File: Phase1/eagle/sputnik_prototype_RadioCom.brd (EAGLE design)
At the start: 100 x 80 mm, 66 parts, among them Y1 32MHz

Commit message: hooked up SPI cache
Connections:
- new net N$12: U$1.29, U$3.2
- new net N$14: U$1.28, U$3.6
- new net N$15: U$1.31, U$3.5
- new net N$23: U$1.58, U$3.7
- new net N$26: U$1.32, U$3.3
- new net N$4: U$1.27, U$3.1
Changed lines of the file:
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@@
 <?xml version="1.0" encoding="utf-8"?>
 <!DOCTYPE eagle SYSTEM "eagle.dtd">
-<eagle version="7.4.0">
+<eagle version="7.3.0">
 <drawing>
 <settings>
@@
 <wire x1="-72.43" y1="-184.15" x2="-76.67" y2="-201.93" width="0" layer="19" extent="1-1"/>
 </signal>
+<signal name="N$4">
+<contactref element="U$1" pad="27"/>
+<contactref element="U$3" pad="1"/>
+<wire x1="-20.2522" y1="10.37" x2="-68.03" y2="-160.81" width="0" layer="19" extent="1-1"/>
+</signal>
+<signal name="N$12">
+<contactref element="U$3" pad="2"/>
+<contactref element="U$1" pad="29"/>
+<wire x1="-20.88" y1="11.4978" x2="-66.76" y2="-160.81" width="0" layer="19" extent="1-1"/>
+</signal>
+<signal name="N$14">
+<contactref element="U$1" pad="28"/>
+<contactref element="U$3" pad="6"/>
+<wire x1="-20.2522" y1="10.87" x2="-65.49" y2="-155.51" width="0" layer="19" extent="1-1"/>
+</signal>
+<signal name="N$15">
+<contactref element="U$1" pad="31"/>
+<contactref element="U$3" pad="5"/>
+<wire x1="-21.88" y1="11.4978" x2="-64.22" y2="-155.51" width="0" layer="19" extent="1-1"/>
+</signal>
+<signal name="N$23">
+<contactref element="U$1" pad="58"/>
+<contactref element="U$3" pad="7"/>
+<wire x1="-22.38" y1="10.37" x2="-66.76" y2="-155.51" width="0" layer="19" extent="1-1"/>
+</signal>
+<signal name="N$26">
+<contactref element="U$1" pad="32"/>
+<contactref element="U$3" pad="3"/>
+<wire x1="-22.38" y1="11.4978" x2="-65.49" y2="-160.81" width="0" layer="19" extent="1-1"/>
+</signal>
 </signals>

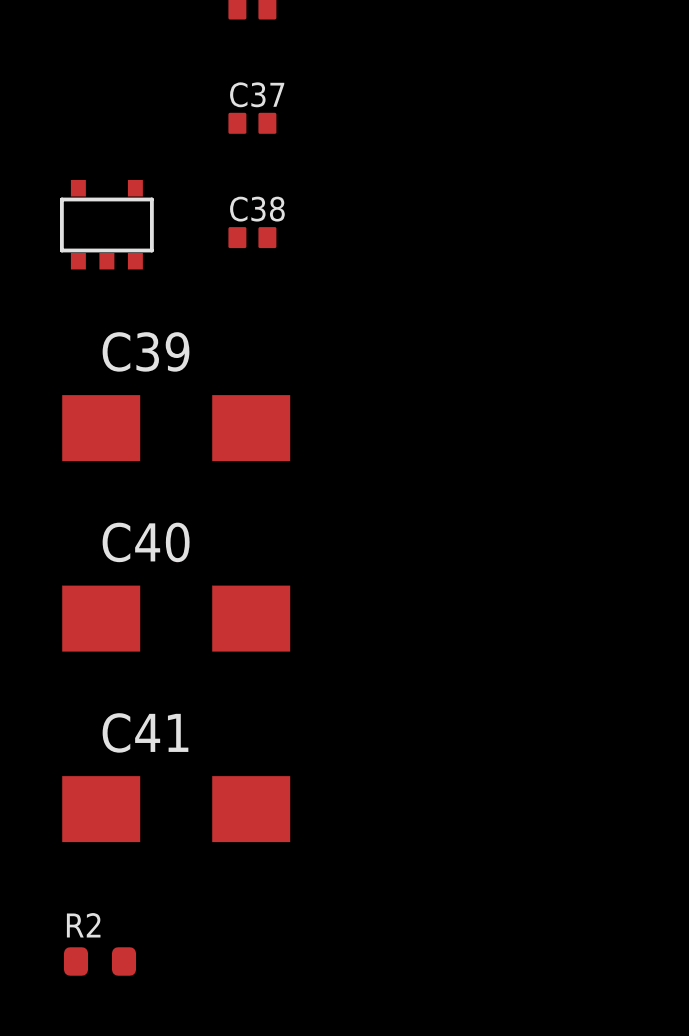
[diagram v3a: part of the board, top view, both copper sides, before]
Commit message: Changed KW0x LDO
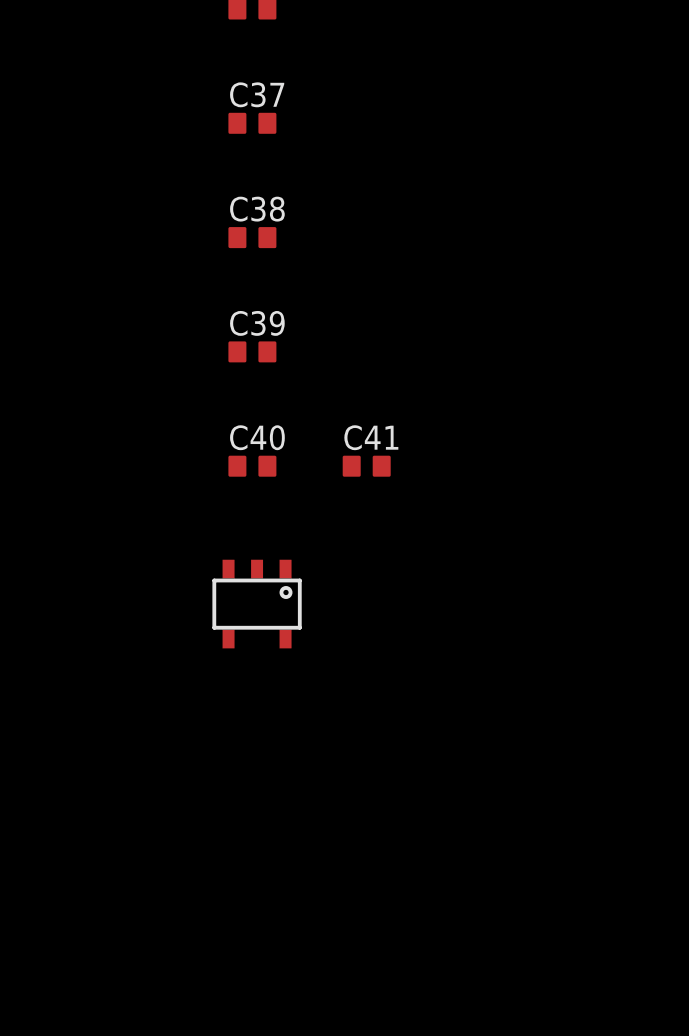
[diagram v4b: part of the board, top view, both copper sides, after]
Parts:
- removed R2: (no value), rcl_custom:.0603-B-NOSILK
- C39: value 4.7uF -> 2.2uF; device rcl:CT6032 -> rcl_custom:.0402-B-NOSILK
- C40: value 1uF -> 10nF; device rcl:CT6032 -> rcl_custom:.0402-B-NOSILK
- C41: value .01uF -> 1uF; device rcl:CT6032 -> rcl_custom:.0402-B-NOSILK
- U$8: value TPS78930DBVT -> AAT3215; device psas_c3_team05:TPS78930DBVT -> psas_c3_team05:AAT3215
- moved U$8 13.7 mm to (-73.7, -189.2)
- moved C41 13.1 mm to (-68.6, -185.4)
- moved C40 5.68 mm to (-72.4, -185.4)
- moved C39 3.59 mm to (-72.4, -181.6)
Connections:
- removed net N$3: C26.1, C27.1, C28.2, C29.2, C39.+, U$1.1, U$1.19, U$1.55, U$1.56, U$8.5
- net 3.3V: no longer C40.+, U$8.1
- net GND: now also C39.2, C40.2, C41.2; no longer C40.-, C41.-, R2.1, U$8.3
- net N$11: now also C26.1, C27.1, C28.2, C29.2, C39.1, U$1.1, U$1.19, U$1.55, U$1.56, U$8.5; no longer C41.+, U$8.4
- net N$13: now also C40.1, U$8.4; no longer C39.-, R2.2
- net V+: now also C41.1, U$8.1
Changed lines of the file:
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@@
 <?xml version="1.0" encoding="utf-8"?>
 <!DOCTYPE eagle SYSTEM "eagle.dtd">
-<eagle version="7.3.0">
+<eagle version="7.4.0">
 <drawing>
 <settings>
@@
 <element name="C37" library="rcl_custom" package=".0402-B-NOSILK" value="10nF" x="-72.39" y="-173.99"/>
 <element name="C38" library="rcl_custom" package=".0402-B-NOSILK" value="1uF" x="-72.39" y="-177.8"/>
-<element name="U$8" library="psas_c3_team05" package="TPS78930DBVT" value="TPS78930DBVT" x="-78.74" y="-176.53"/>
-<element name="C39" library="rcl" package="CT6032" value="4.7uF" x="-74.93" y="-184.15"/>
-<element name="C40" library="rcl" package="CT6032" value="1uF" x="-74.93" y="-190.5"/>
-<element name="C41" library="rcl" package="CT6032" value=".01uF" x="-74.93" y="-196.85"/>
-<element name="R2" library="rcl_custom" package=".0603-B-NOSILK" value="" x="-77.47" y="-201.93"/>
+<element name="U$8" library="psas_c3_team05" package="AAT3215" value="AAT3215" x="-73.66" y="-189.23"/>
+<element name="C39" library="rcl_custom" package=".0402-B-NOSILK" value="2.2uF" x="-72.39" y="-181.61"/>
+<element name="C40" library="rcl_custom" package=".0402-B-NOSILK" value="10nF" x="-72.39" y="-185.42"/>
+<element name="C41" library="rcl_custom" package=".0402-B-NOSILK" value="1uF" x="-68.58" y="-185.42"/>
 </elements>
 <signals>
@@
 <contactref element="U$3" pad="4"/>
 <contactref element="U$8" pad="2"/>
-<contactref element="U$8" pad="3"/>
-<contactref element="C41" pad="-"/>
-<contactref element="C40" pad="-"/>
-<contactref element="R2" pad="1"/>
+<contactref element="C41" pad="2"/>
+<contactref element="C39" pad="2"/>
+<contactref element="C40" pad="2"/>
+<wire x1="-71.89" y1="-185.42" x2="-68.08" y2="-185.42" width="0" layer="19" extent="1-1"/>
+<wire x1="-72.235" y1="-188.85" x2="-71.89" y2="-185.42" width="0" layer="19" extent="1-1"/>
+<wire x1="-71.89" y1="-181.61" x2="-71.89" y2="-185.42" width="0" layer="19" extent="1-1"/>
+<wire x1="-71.89" y1="-177.8" x2="-71.89" y2="-181.61" width="0" layer="19" extent="1-1"/>
 <wire x1="-71.89" y1="-173.99" x2="-71.89" y2="-177.8" width="0" layer="19" extent="1-1"/>
 <wire x1="-71.89" y1="-170.18" x2="-71.89" y2="-173.99" width="0" layer="19" extent="1-1"/>
-<wire x1="-76.29" y1="-178.587" x2="-71.89" y2="-177.8" width="0" layer="19" extent="1-1"/>
-<wire x1="-77.24" y1="-178.587" x2="-76.29" y2="-178.587" width="0" layer="19" extent="1-1"/>
 <wire x1="-72.235" y1="-164.72" x2="-71.89" y2="-170.18" width="0" layer="19" extent="1-1"/>
 <wire x1="-64.77" y1="-166.37" x2="-72.235" y2="-164.72" width="0" layer="19" extent="1-1"/>
@@
 <wire x1="-61.76" y1="-154.94" x2="-61.76" y2="-160.02" width="0" layer="19" extent="1-1"/>
 <wire x1="-60.03" y1="-151.502" x2="-61.76" y2="-154.94" width="0" layer="19" extent="1-1"/>
-<wire x1="-72.43" y1="-190.5" x2="-76.29" y2="-178.587" width="0" layer="19" extent="1-1"/>
-<wire x1="-72.43" y1="-196.85" x2="-72.43" y2="-190.5" width="0" layer="19" extent="1-1"/>
-<wire x1="-78.27" y1="-201.93" x2="-72.43" y2="-196.85" width="0" layer="19" extent="1-1"/>
 <wire x1="-50.84" y1="-129.54" x2="-60.03" y2="-151.502" width="0" layer="19" extent="1-1"/>
 <wire x1="-56.65" y1="-119.38" x2="-50.84" y2="-129.54" width="0" layer="19" extent="1-1"/>
@@
 <contactref element="C38" pad="1"/>
 <contactref element="U$7" pad="1"/>
+<contactref element="C41" pad="1"/>
+<contactref element="U$8" pad="1"/>
+<wire x1="-69.08" y1="-185.42" x2="-72.89" y2="-177.8" width="0" layer="19" extent="1-1"/>
+<wire x1="-71.285" y1="-188.85" x2="-69.08" y2="-185.42" width="0" layer="19" extent="1-1"/>
 <wire x1="-67.31" y1="-166.37" x2="-72.89" y2="-177.8" width="0" layer="19" extent="1-1"/>
 <wire x1="-71.285" y1="-164.72" x2="-67.31" y2="-166.37" width="0" layer="19" extent="1-1"/>
@@
 <contactref element="J1" pad="1"/>
 <contactref element="U$3" pad="8"/>
-<contactref element="C40" pad="+"/>
-<contactref element="U$8" pad="1"/>
-<wire x1="-78.19" y1="-178.587" x2="-68.03" y2="-155.51" width="0" layer="19" extent="1-1"/>
-<wire x1="-77.43" y1="-190.5" x2="-78.19" y2="-178.587" width="0" layer="19" extent="1-1"/>
 <wire x1="-28.0078" y1="10.87" x2="-68.03" y2="-155.51" width="0" layer="19" extent="1-1"/>
 <wire x1="-23.88" y1="11.4978" x2="-28.0078" y2="10.87" width="0" layer="19" extent="1-1"/>
@@
 <wire x1="-71.285" y1="-167.05" x2="-72.89" y2="-170.18" width="0" layer="19" extent="1-1"/>
 </signal>
-<signal name="N$3">
+<signal name="N$4">
+<contactref element="U$1" pad="27"/>
+<contactref element="U$3" pad="1"/>
+<wire x1="-20.2522" y1="10.37" x2="-68.03" y2="-160.81" width="0" layer="19" extent="1-1"/>
+</signal>
+<signal name="N$12">
+<contactref element="U$3" pad="2"/>
+<contactref element="U$1" pad="29"/>
+<wire x1="-20.88" y1="11.4978" x2="-66.76" y2="-160.81" width="0" layer="19" extent="1-1"/>
+</signal>
+<signal name="N$14">
+<contactref element="U$1" pad="28"/>
+<contactref element="U$3" pad="6"/>
+<wire x1="-20.2522" y1="10.87" x2="-65.49" y2="-155.51" width="0" layer="19" extent="1-1"/>
+</signal>
+<signal name="N$15">
+<contactref element="U$1" pad="31"/>
+<contactref element="U$3" pad="5"/>
+<wire x1="-21.88" y1="11.4978" x2="-64.22" y2="-155.51" width="0" layer="19" extent="1-1"/>
+</signal>
+<signal name="N$23">
+<contactref element="U$1" pad="58"/>
+<contactref element="U$3" pad="7"/>
+<wire x1="-22.38" y1="10.37" x2="-66.76" y2="-155.51" width="0" layer="19" extent="1-1"/>
+</signal>
+<signal name="N$26">
+<contactref element="U$1" pad="32"/>
+<contactref element="U$3" pad="3"/>
+<wire x1="-22.38" y1="11.4978" x2="-65.49" y2="-160.81" width="0" layer="19" extent="1-1"/>
+</signal>
+<signal name="N$11">
+<contactref element="U$8" pad="5"/>
+<contactref element="C39" pad="1"/>
+<contactref element="U$1" pad="19"/>
+<contactref element="C27" pad="1"/>
 <contactref element="U$1" pad="1"/>
-<contactref element="C27" pad="1"/>
-<contactref element="U$1" pad="19"/>
+<contactref element="C28" pad="2"/>
+<contactref element="C26" pad="1"/>
 <contactref element="U$1" pad="55"/>
+<contactref element="U$1" pad="56"/>
 <contactref element="C29" pad="2"/>
-<contactref element="U$1" pad="56"/>
-<contactref element="C26" pad="1"/>
-<contactref element="C28" pad="2"/>
-<contactref element="U$8" pad="5"/>
-<contactref element="C39" pad="+"/>
-<wire x1="-77.43" y1="-184.15" x2="-78.19" y2="-176.155" width="0" layer="19" extent="1-1"/>
-<wire x1="-27.38" y1="3.7422" x2="-78.19" y2="-176.155" width="0" layer="19" extent="1-1"/>
+<wire x1="-71.285" y1="-191.18" x2="-72.89" y2="-181.61" width="0" layer="19" extent="1-1"/>
+<wire x1="-27.38" y1="3.7422" x2="-72.89" y2="-181.61" width="0" layer="19" extent="1-1"/>
 <wire x1="-28.0078" y1="4.37" x2="-27.38" y2="3.7422" width="0" layer="19" extent="1-1"/>
 <wire x1="-28.0078" y1="4.87" x2="-28.0078" y2="4.37" width="0" layer="19" extent="1-1"/>
@@
 <wire x1="-42.38" y1="31.75" x2="-37.3" y2="31.75" width="0" layer="19" extent="1-1"/>
 </signal>
-<signal name="N$11">
+<signal name="N$13">
 <contactref element="U$8" pad="4"/>
-<contactref element="C41" pad="+"/>
-<wire x1="-77.43" y1="-196.85" x2="-76.29" y2="-176.155" width="0" layer="19" extent="1-1"/>
-</signal>
-<signal name="N$13">
-<contactref element="C39" pad="-"/>
-<contactref element="R2" pad="2"/>
-<wire x1="-72.43" y1="-184.15" x2="-76.67" y2="-201.93" width="0" layer="19" extent="1-1"/>
-</signal>
-<signal name="N$4">
-<contactref element="U$1" pad="27"/>
-<contactref element="U$3" pad="1"/>
-<wire x1="-20.2522" y1="10.37" x2="-68.03" y2="-160.81" width="0" layer="19" extent="1-1"/>
-</signal>
-<signal name="N$12">
-<contactref element="U$3" pad="2"/>
-<contactref element="U$1" pad="29"/>
-<wire x1="-20.88" y1="11.4978" x2="-66.76" y2="-160.81" width="0" layer="19" extent="1-1"/>
-</signal>
-<signal name="N$14">
-<contactref element="U$1" pad="28"/>
-<contactref element="U$3" pad="6"/>
-<wire x1="-20.2522" y1="10.87" x2="-65.49" y2="-155.51" width="0" layer="19" extent="1-1"/>
-</signal>
-<signal name="N$15">
-<contactref element="U$1" pad="31"/>
-<contactref element="U$3" pad="5"/>
-<wire x1="-21.88" y1="11.4978" x2="-64.22" y2="-155.51" width="0" layer="19" extent="1-1"/>
-</signal>
-<signal name="N$23">
-<contactref element="U$1" pad="58"/>
-<contactref element="U$3" pad="7"/>
-<wire x1="-22.38" y1="10.37" x2="-66.76" y2="-155.51" width="0" layer="19" extent="1-1"/>
-</signal>
-<signal name="N$26">
-<contactref element="U$1" pad="32"/>
-<contactref element="U$3" pad="3"/>
-<wire x1="-22.38" y1="11.4978" x2="-65.49" y2="-160.81" width="0" layer="19" extent="1-1"/>
+<contactref element="C40" pad="1"/>
+<wire x1="-72.89" y1="-185.42" x2="-73.185" y2="-191.18" width="0" layer="19" extent="1-1"/>
 </signal>
 </signals>

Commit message: added attributes to several parts, started organizing the board to prep for layout
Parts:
- removed U$1: MKW01Z128, psas_c3_team05:MKW01Z128
- removed U$2: SMAJ716-ND, psas_c3_team05:SMAJ716-ND
- removed U$3: LE25FU406B, psas_c3_team05:LE25FU406B
- removed U$4: MAAL-010704, sputnik:MAAL-010704
- removed U$5: SKY13405-490LF, psas_c3_team05:SKY13405-490LF
- removed U$6: SKY65116, psas_c3_team05:SKY65116
- added CACHE: LE25FU406B, psas_c3_team05:LE25FU406B
- added KW0X: MKW01Z128, psas_c3_team05:MKW01Z128
- added LNA: MAAL-010704, sputnik:MAAL-010704
- added PA: SKY65116, psas_c3_team05:SKY65116
- added SMA: SMAJ716-ND, psas_c3_team05:SMAJ716-ND
- added TP1, TP2, TP3, TP4, TP5, TP6, TP7, TP8: TPSPAD1-13, testpad:P1-13
- added TRSWITCH: SKY13405-490LF, psas_c3_team05:SKY13405-490LF
- moved C36 271.6 mm to (41.9, 76.2)
- moved C37 271.6 mm to (41.9, 72.4)
- moved C38 271.6 mm to (41.9, 68.6)
- moved C39 271.6 mm to (41.9, 64.8)
- moved C40 271.6 mm to (41.9, 61.0)
- moved C41 271.6 mm to (45.7, 61.0)
- moved JP1 263.0 mm to (35.6, 76.2)
- moved U$8 260.0 mm to (29.2, 49.5)
- moved C13 243.9 mm to (66.0, 53.3)
- moved C46 243.9 mm to (66.0, 48.3)
- moved U$9 240.3 mm to (77.5, 47.0)
- moved U$7 235.3 mm to (61.0, 27.9)
- moved C23 212.6 mm to (29.2, 78.7)
- moved C24 212.6 mm to (29.2, 74.9)
- moved C25 212.6 mm to (29.2, 71.1)
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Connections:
- net 3.3V: now also CACHE.8, KW0X.35, KW0X.43; no longer U$1.35, U$1.43, U$3.8
- net DIO5/CLKOUT: now also KW0X.15, KW0X.54; no longer U$1.15, U$1.54
- net GND: now also CACHE.4, KW0X.2, KW0X.20, KW0X.3, KW0X.36, KW0X.38, KW0X.4, KW0X.40, KW0X.PGND1, KW0X.PGND2, LNA.2, LNA.5, PA.1, PA.3, PA.5, PA.6, PA.7, PA.9, SMA.GND1, SMA.GND2, SMA.GND3, SMA.GND4, TRSWITCH.1, TRSWITCH.11, TRSWITCH.3, TRSWITCH.4, TRSWITCH.6, TRSWITCH.7, TRSWITCH.9; no longer U$1.2, U$1.20, U$1.3, U$1.36, U$1.38, U$1.4, U$1.40, U$1.PGND1, U$1.PGND2, U$2.GND1, U$2.GND2, U$2.GND3, U$2.GND4, U$3.4, U$4.2, U$4.5, U$5.1, U$5.11, U$5.3, U$5.4, U$5.6, U$5.7, U$5.9, U$6.1, U$6.3, U$6.5, U$6.6, U$6.7, U$6.9
- net N$11: now also KW0X.1, KW0X.19, KW0X.55, KW0X.56; no longer U$1.1, U$1.19, U$1.55, U$1.56
- net N$12: now also CACHE.2, KW0X.29, TP4.TP; no longer U$1.29, U$3.2
- net N$14: now also CACHE.6, KW0X.28, TP3.TP; no longer U$1.28, U$3.6
- net N$15: now also CACHE.5, KW0X.31, TP5.TP; no longer U$1.31, U$3.5
- net N$21: now also PA.2; no longer U$6.2
- net N$22: now also PA.8, TRSWITCH.2; no longer U$5.2, U$6.8
- net N$23: now also CACHE.7, KW0X.58, TP1.TP; no longer U$1.58, U$3.7
- net N$24: now also LNA.3; no longer U$4.3
- net N$26: now also CACHE.3, KW0X.32; no longer U$1.32, U$3.3
- net N$27: now also LNA.4; no longer U$4.4
- net N$29: now also KW0X.42; no longer U$1.42
- net N$30: now also SMA.P$3, TRSWITCH.5; no longer U$2.P$3, U$5.5
- net N$31: now also KW0X.44; no longer U$1.44
- net N$34: now also KW0X.45; no longer U$1.45
- net N$4: now also CACHE.1, KW0X.27, TP2.TP; no longer U$1.27, U$3.1
- net N$5: now also TRSWITCH.8; no longer U$5.8
- net N$6: now also KW0X.46; no longer U$1.46
- net N$7: now also LNA.6; no longer U$4.6
- net N$8: now also KW0X.47; no longer U$1.47
- net PA_BOOST: now also KW0X.41; no longer U$1.41
- net PE0/UART0RX: now also KW0X.13, TP7.TP; no longer U$1.13
- net PE1/UART0TX: now also KW0X.14, TP6.TP; no longer U$1.14
- net PE3: now also KW0X.33, TP8.TP; no longer U$1.33
- net PTA0: now also KW0X.10; no longer U$1.10
- net PTA3: now also KW0X.11; no longer U$1.11
- net RFIO: now also KW0X.39; no longer U$1.39
- net RXTX: now also KW0X.37, TRSWITCH.12; no longer U$1.37, U$5.12
- net V+: now also TRSWITCH.10; no longer U$5.10
- net VPA: now also PA.10, PA.11, PA.12, PA.4; no longer U$6.10, U$6.11, U$6.12, U$6.4

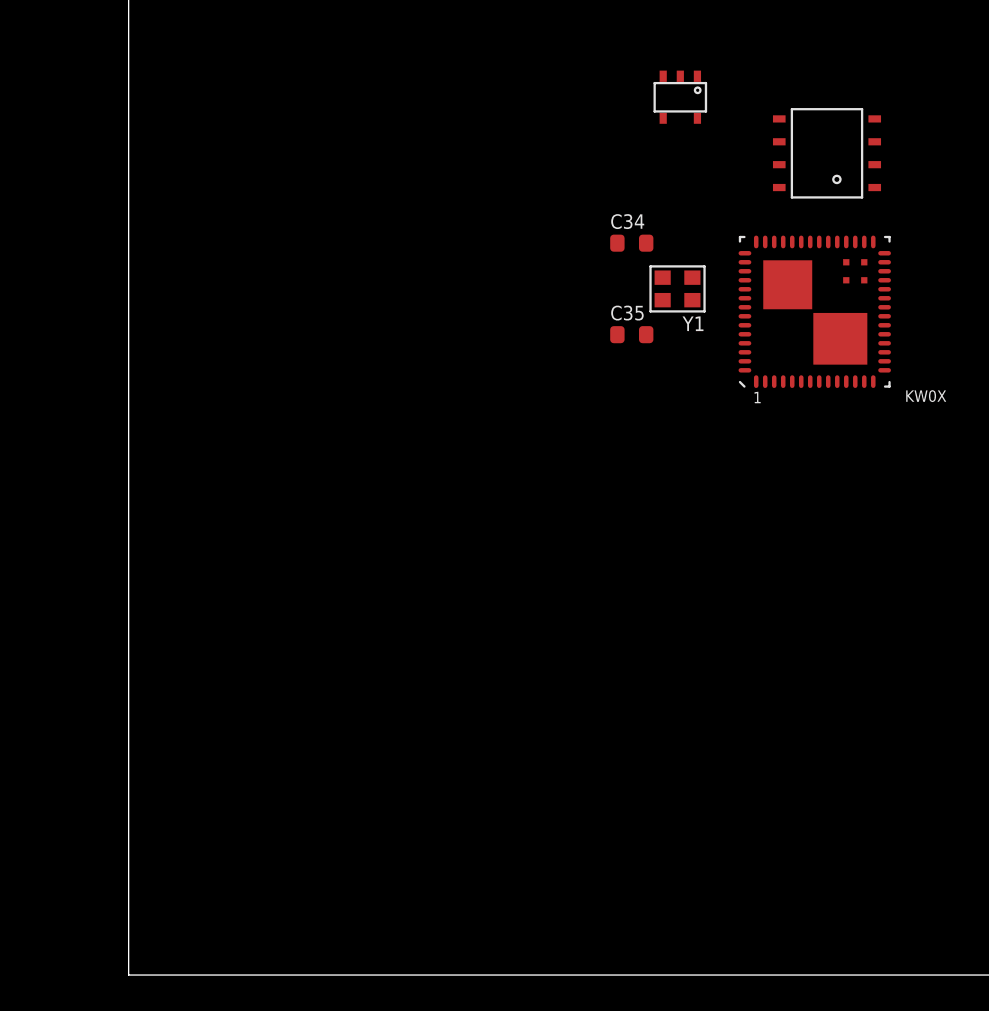
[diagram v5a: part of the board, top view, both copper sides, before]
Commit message: Fixed OIs, fixed SysCon LDO, replaced SPI cache
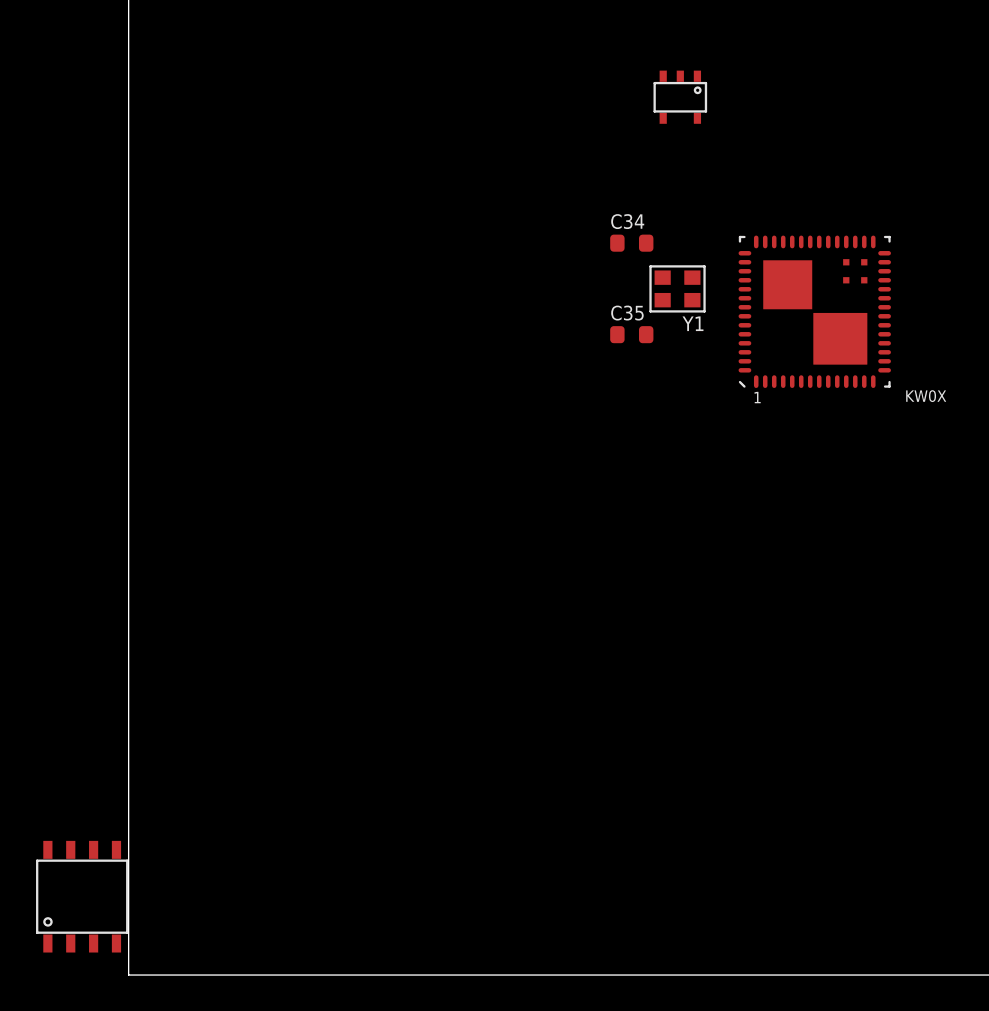
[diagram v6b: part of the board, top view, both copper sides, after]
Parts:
- removed CACHE: LE25FU406B, psas_c3_team05:LE25FU406B
- added U$1: W25Q80DV, psas_c3_team05:W25Q80DV
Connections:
- removed net N$4: CACHE.1, KW0X.27, TP2.TP
- new net N$28: KW0X.27, TP2.TP, U$1.1
- net 3.3V: no longer CACHE.8
- net GND: now also U$1.4; no longer CACHE.4
- net N$12: now also U$1.2; no longer CACHE.2
- net N$14: now also U$1.6; no longer CACHE.6
- net N$15: now also U$1.5; no longer CACHE.5
- net N$23: now also U$1.7; no longer CACHE.7
- net N$26: now also U$1.3; no longer CACHE.3
- net V+: now also U$1.8
